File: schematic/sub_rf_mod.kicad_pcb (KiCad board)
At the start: 2 copper layers, 69.1 x 50 mm, 39 parts, among them J4B1 Conn_01x08

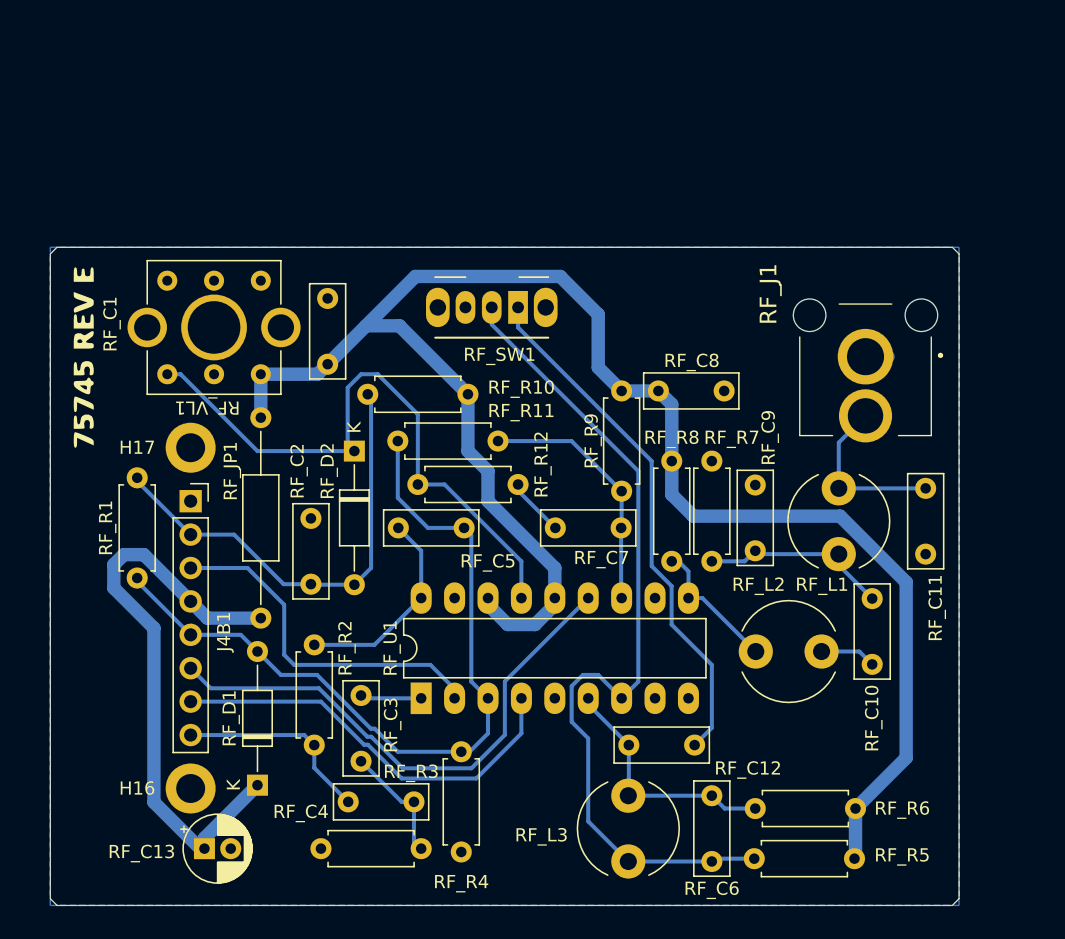
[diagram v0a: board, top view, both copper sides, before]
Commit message: fixed footprint lead size
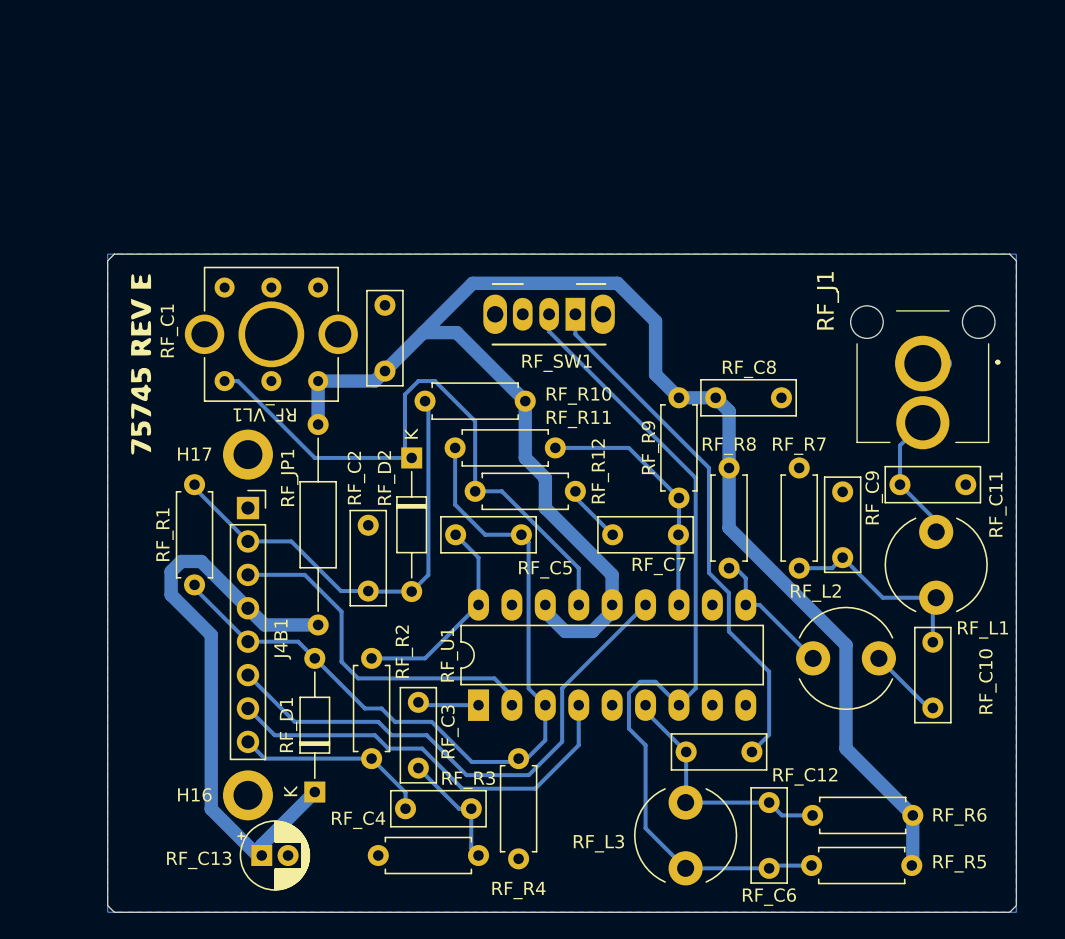
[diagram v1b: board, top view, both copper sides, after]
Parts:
- moved RF_L1 8.11 mm to (172.5, 96.7)
- moved RF_C9 6.66 mm to (165.4, 93.7)
- moved RF_R7 6.66 mm to (162.1, 94.5)
- moved RF_C10 5.68 mm to (172.3, 105.1)
- moved RF_R2 4.48 mm to (129.6, 101.3)
- moved H16 4.39 mm to (120.2, 111.8)
- moved H17 4.39 mm to (120.2, 85.9)
- moved RF_C3 4.39 mm to (133.1, 104.7)
- moved RF_C6 4.39 mm to (159.8, 117.3)
- moved RF_C8 4.39 mm to (155.7, 81.5)
- moved RF_D1 4.39 mm to (125.3, 111.5)
- moved RF_J1 4.39 mm to (171.5, 78.9)
- moved RF_JP1 4.39 mm to (125.5, 83.6)
- moved RF_L2 4.39 mm to (163.1, 101.3)
- moved RF_R12 4.39 mm to (145.1, 88.6)
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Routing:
- net (no net): track 651.3 -> 641.1 mm

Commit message: changed switch to one that is a better match for the old (larger)
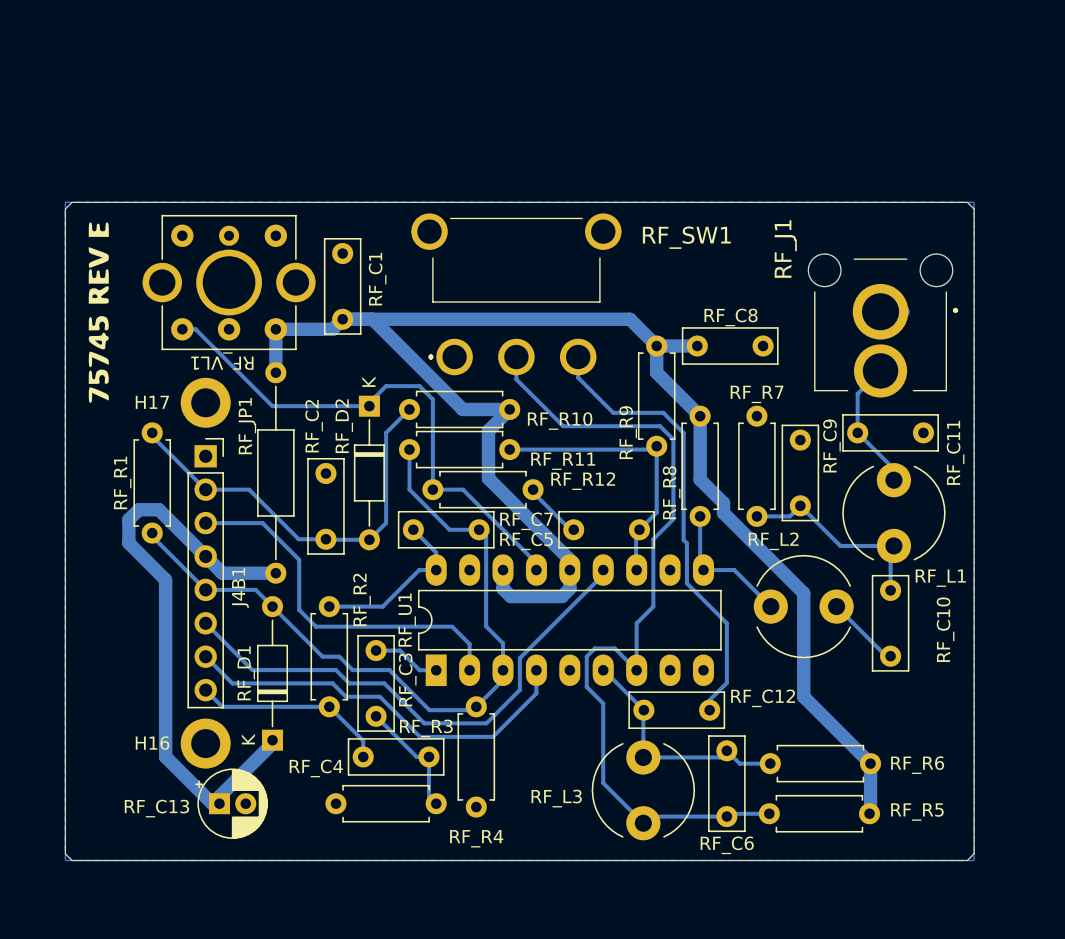
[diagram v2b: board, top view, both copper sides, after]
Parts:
- RF_SW1: footprint Switches_THT:SW_CuK_OS102011MA1QN1_SPDT_Angled -> 1101M2S3ABE2:1101M2S3ABE2
- moved RF_SW1 9.74 mm to (135.9, 78.4)
- moved H16 5.08 mm to (117.0, 107.8)
- moved RF_C11 5.08 mm to (166.5, 84.2)
- moved RF_C6 5.08 mm to (156.6, 113.4)
- moved RF_C9 5.08 mm to (162.2, 89.7)
- moved RF_R6 5.08 mm to (159.9, 109.3)
- moved RF_R2 5.08 mm to (126.4, 97.4)
- moved H17 5.08 mm to (117.0, 81.9)
- moved J4B1 5.08 mm to (117.0, 86.0)
- moved RF_C1 5.08 mm to (127.4, 75.6)
- moved RF_C10 5.08 mm to (169.0, 101.2)
- moved RF_C3 5.08 mm to (129.9, 100.8)
- moved RF_C4 5.08 mm to (133.9, 108.8)
- moved RF_D1 5.08 mm to (122.0, 107.6)
- moved RF_J1 5.08 mm to (168.3, 75.0)
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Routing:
- net (no net): track 641.1 -> 614.5 mm

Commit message: update routing of rf board to fix loop over pin
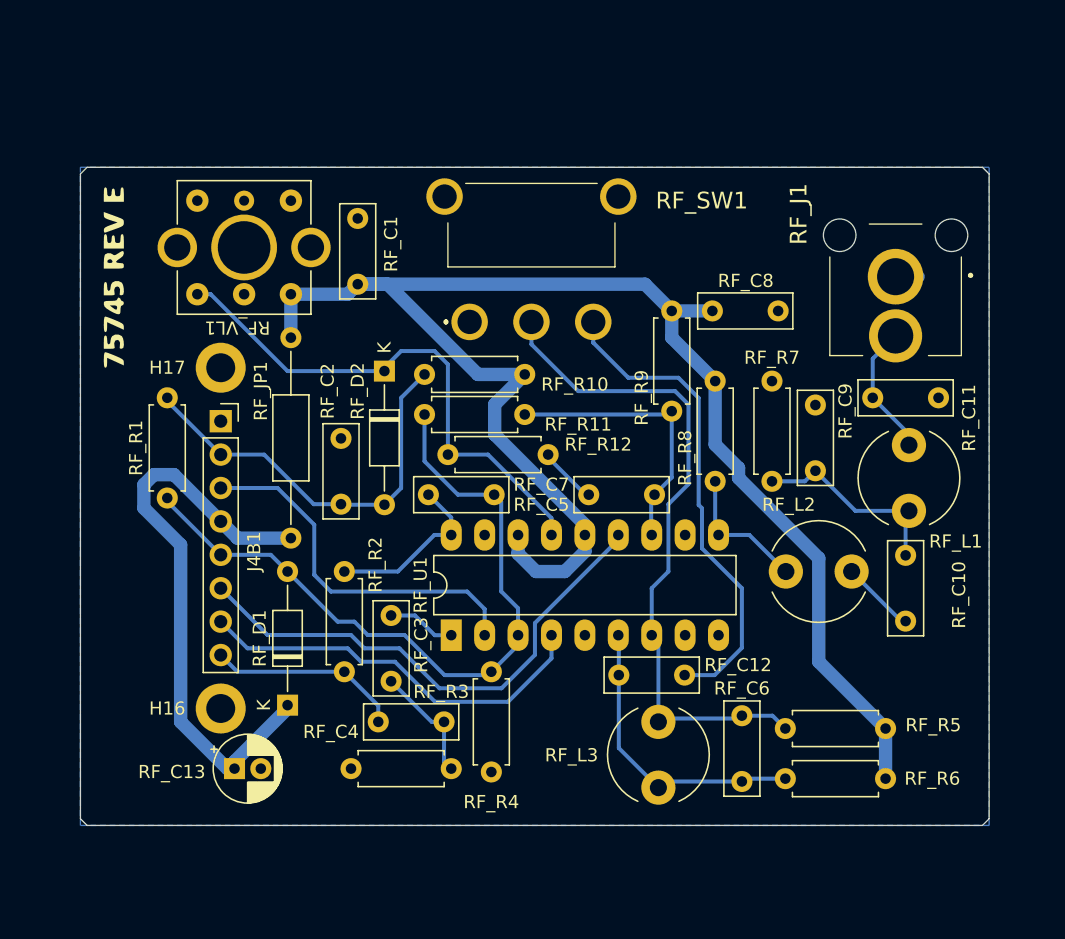
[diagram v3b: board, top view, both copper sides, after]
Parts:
- moved RF_L3 7.79 mm to (151.4, 106.2), turned to -90 degrees
- moved RF_C6 7.75 mm to (157.7, 105.7), turned to -90 degrees
- moved RF_R5 6.59 mm to (168.7, 106.7)
- moved RF_C12 3.28 mm to (153.4, 102.6)
- moved H17 2.90 mm to (118.1, 79.2)
- moved J4B1 2.90 mm to (118.1, 83.3)
- moved RF_C1 2.90 mm to (128.5, 72.9)
- moved RF_C10 2.90 mm to (170.2, 98.5)
- moved RF_C13 2.90 mm to (119.2, 109.7)
- moved RF_C2 2.90 mm to (127.3, 84.6)
- moved RF_C3 2.90 mm to (131.1, 98.1)
- moved RF_C4 2.90 mm to (135.1, 106.2)
- moved RF_C9 2.90 mm to (163.3, 87.1)
- moved RF_D1 2.90 mm to (123.2, 104.9)
- moved RF_D2 2.90 mm to (130.6, 79.5)
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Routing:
- net (no net): track 614.5 -> 612.3 mm

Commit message: cleanup for release of version 1
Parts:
- moved RF_C3 7.90 mm to (134.7, 91.1)
- moved RF_L3 7.90 mm to (155.1, 99.2)
- moved RF_R10 7.90 mm to (144.9, 72.8)
- moved RF_R3 7.90 mm to (131.7, 102.7)
- moved RF_C8 7.90 mm to (159.2, 67.9)
- moved RF_R5 7.90 mm to (172.3, 99.7)
- moved RF_R9 7.90 mm to (156.1, 67.9)
- moved H16 7.90 mm to (121.8, 98.2)
- moved H17 7.90 mm to (121.8, 72.3)
- moved J4B1 7.90 mm to (121.8, 76.3)
- moved RF_C2 7.90 mm to (130.9, 77.6)
- moved RF_D1 7.90 mm to (126.9, 97.9)
- moved RF_R2 7.90 mm to (131.2, 87.8)
- moved S5 7.90 mm to (113.7, 65.4)
- moved RF_C1 7.90 mm to (132.2, 65.9)
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
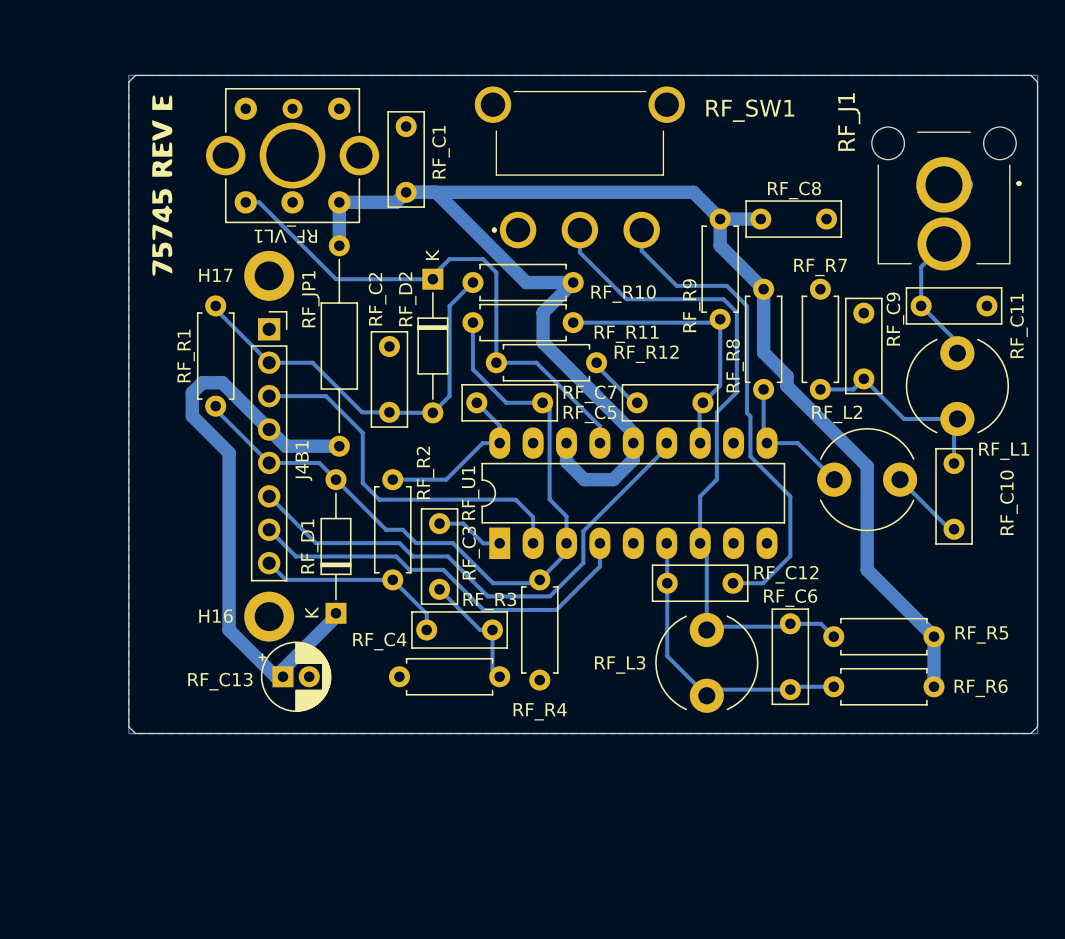
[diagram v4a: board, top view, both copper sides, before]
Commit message: made sure all schematic parts are up to date
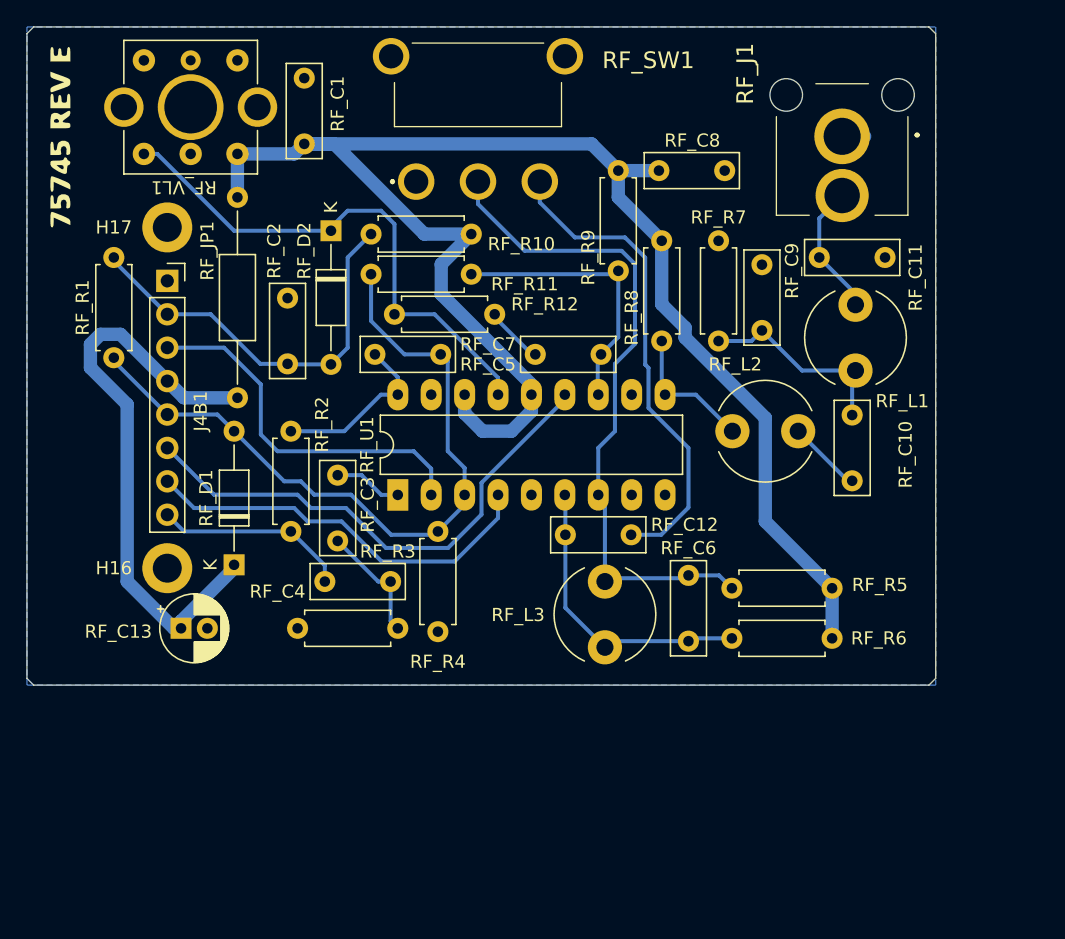
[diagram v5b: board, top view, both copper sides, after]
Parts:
- moved RF_C2 8.58 mm to (123.2, 74.0)
- moved RF_C3 8.58 mm to (127.0, 87.4)
- moved RF_R10 8.58 mm to (137.2, 69.1)
- moved RF_R11 8.58 mm to (129.5, 72.1)
- moved RF_R12 8.58 mm to (138.9, 75.2)
- moved RF_R7 8.58 mm to (156.0, 77.2)
- moved RF_C6 8.58 mm to (153.7, 95.0)
- moved RF_L3 8.58 mm to (147.3, 95.5)
- moved RF_R3 8.58 mm to (124.0, 99.1)
- moved H16 8.58 mm to (114.0, 94.5)
- moved H17 8.58 mm to (114.0, 68.6)
- moved RF_D1 8.58 mm to (119.1, 94.2)
- moved RF_JP1 8.58 mm to (119.4, 66.3)
- moved RF_R2 8.58 mm to (123.4, 84.1)
- moved RF_C1 8.58 mm to (124.5, 62.2)
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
